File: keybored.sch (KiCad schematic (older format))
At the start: 24 parts, among them SW1 SW_Push, U1 ATmega32U4-AU, Y1 16MHz

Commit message: Fixed mx switch footprint to use MX-1U instead of MX-NoLED
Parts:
- MX1, MX2, MX3, MX4: footprint MX_Alps_Hybrid:MX-1U-NoLED -> MX_Alps_Hybrid:MX-1U
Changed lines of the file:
@@
 F 0 "MX1" H 6933 3573 60  0000 C CNN
 F 1 "MX-NoLED" H 6933 3499 20  0000 C CNN
-F 2 "MX_Alps_Hybrid:MX-1U-NoLED" H 6275 3325 60  0001 C CNN
+F 2 "MX_Alps_Hybrid:MX-1U" H 6275 3325 60  0001 C CNN
 F 3 "" H 6275 3325 60  0001 C CNN
 	1    6900 3350
@@
 F 0 "MX2" H 6933 4223 60  0000 C CNN
 F 1 "MX-NoLED" H 6933 4149 20  0000 C CNN
-F 2 "MX_Alps_Hybrid:MX-1U-NoLED" H 6275 3975 60  0001 C CNN
+F 2 "MX_Alps_Hybrid:MX-1U" H 6275 3975 60  0001 C CNN
 F 3 "" H 6275 3975 60  0001 C CNN
 	1    6900 4000
@@
 F 0 "MX4" H 7533 4223 60  0000 C CNN
 F 1 "MX-NoLED" H 7533 4149 20  0000 C CNN
-F 2 "MX_Alps_Hybrid:MX-1U-NoLED" H 6875 3975 60  0001 C CNN
+F 2 "MX_Alps_Hybrid:MX-1U" H 6875 3975 60  0001 C CNN
 F 3 "" H 6875 3975 60  0001 C CNN
 	1    7500 4000
@@
 F 0 "MX3" H 7533 3573 60  0000 C CNN
 F 1 "MX-NoLED" H 7533 3499 20  0000 C CNN
-F 2 "MX_Alps_Hybrid:MX-1U-NoLED" H 6875 3325 60  0001 C CNN
+F 2 "MX_Alps_Hybrid:MX-1U" H 6875 3325 60  0001 C CNN
 F 3 "" H 6875 3325 60  0001 C CNN
 	1    7500 3350

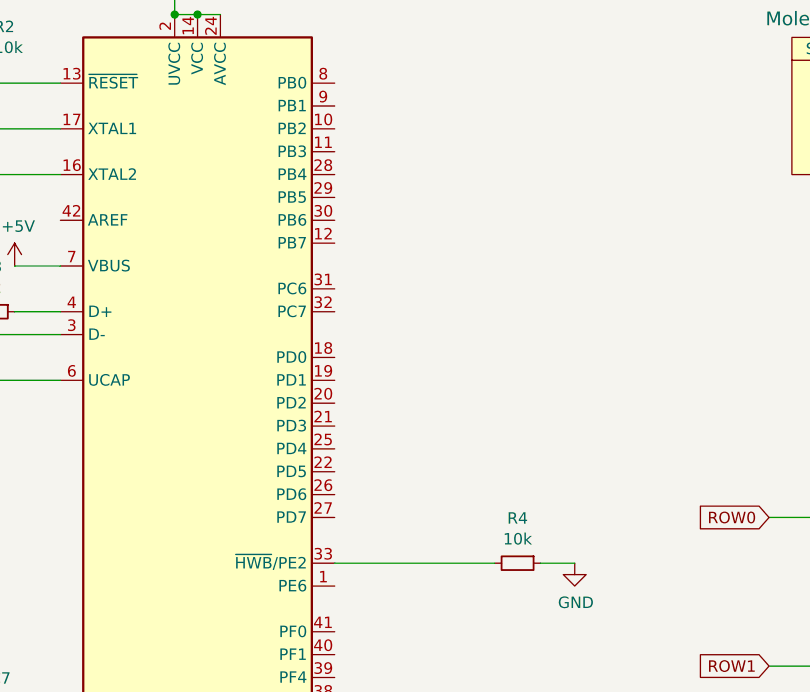
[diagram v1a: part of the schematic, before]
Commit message: completed the v0.1 pcb design
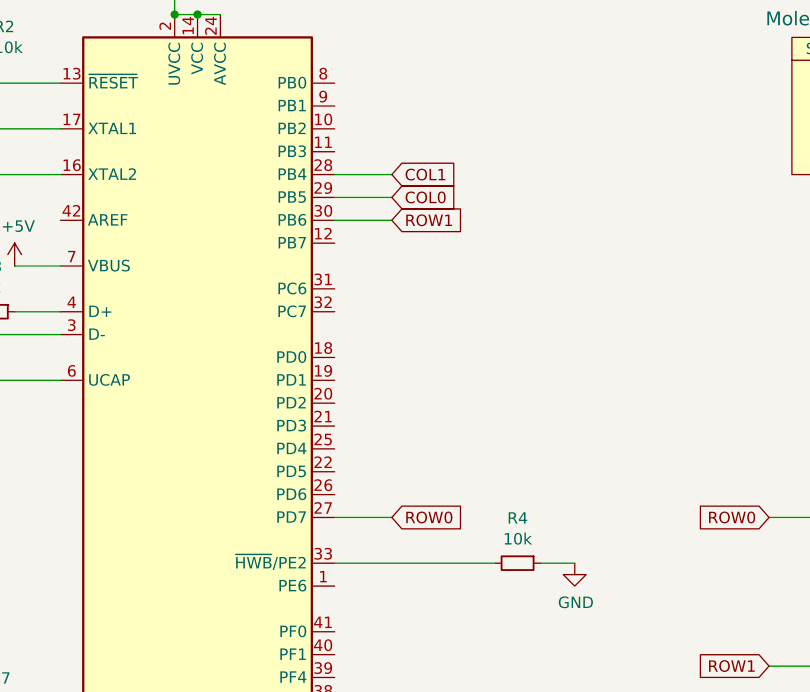
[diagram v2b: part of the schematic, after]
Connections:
- net COL0: now also U1.29 (PB5)
- net COL1: now also U1.28 (PB4)
- net ROW0: now also U1.27 (PD7)
- net ROW1: now also U1.30 (PB6)
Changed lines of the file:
@@
 Text GLabel 7650 2850 1    50   Input ~ 0
 COL1
+Text GLabel 4550 2200 2    50   Input ~ 0
+COL1
+Text GLabel 4550 2300 2    50   Input ~ 0
+COL0
+Text GLabel 4550 2400 2    50   Input ~ 0
+ROW1
+Text GLabel 4550 3700 2    50   Input ~ 0
+ROW0
+Wire Wire Line
+	4550 3700 4300 3700
+Wire Wire Line
+	4550 2400 4300 2400
+Wire Wire Line
+	4550 2300 4300 2300
+Wire Wire Line
+	4550 2200 4300 2200
 $EndSCHEMATC
